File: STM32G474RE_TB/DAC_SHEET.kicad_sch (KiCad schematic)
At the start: 16 parts, among them U2 MCP4921-ESN, U3 MCP4921-ESN, U4 MCP4921-ESN, U5 OPA1678, U6 MCP4921-ESN, U7 REF3125, U9 OPA1678

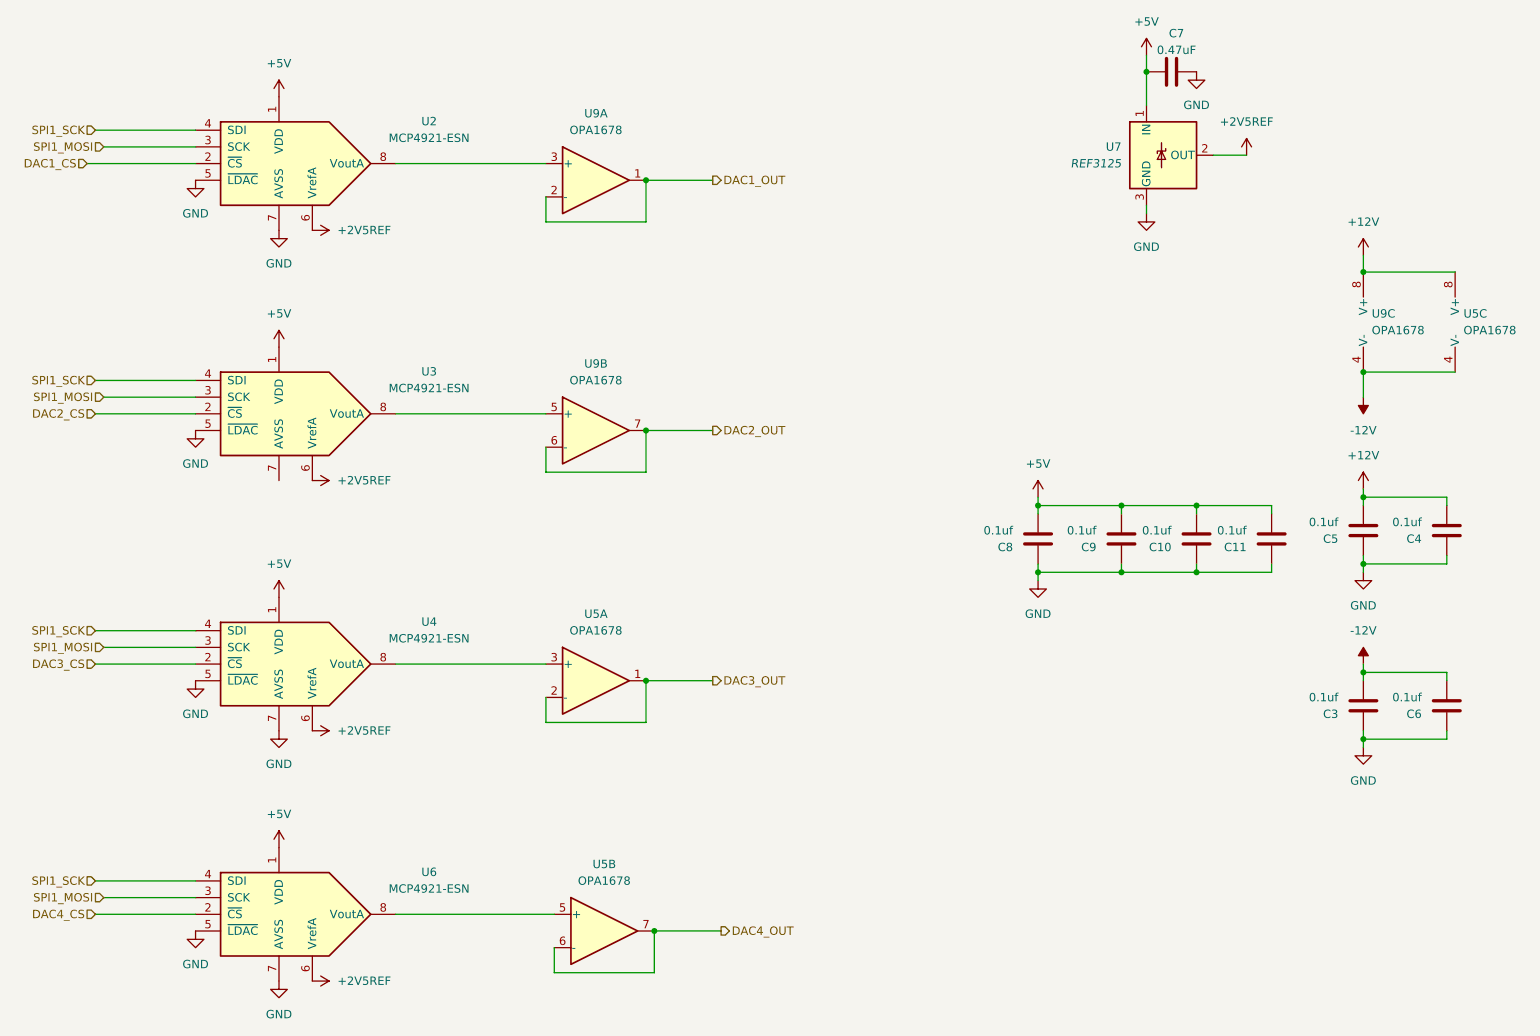
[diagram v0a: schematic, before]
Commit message: Added power LDO and built DAC buffer circuits Added pin descriptions
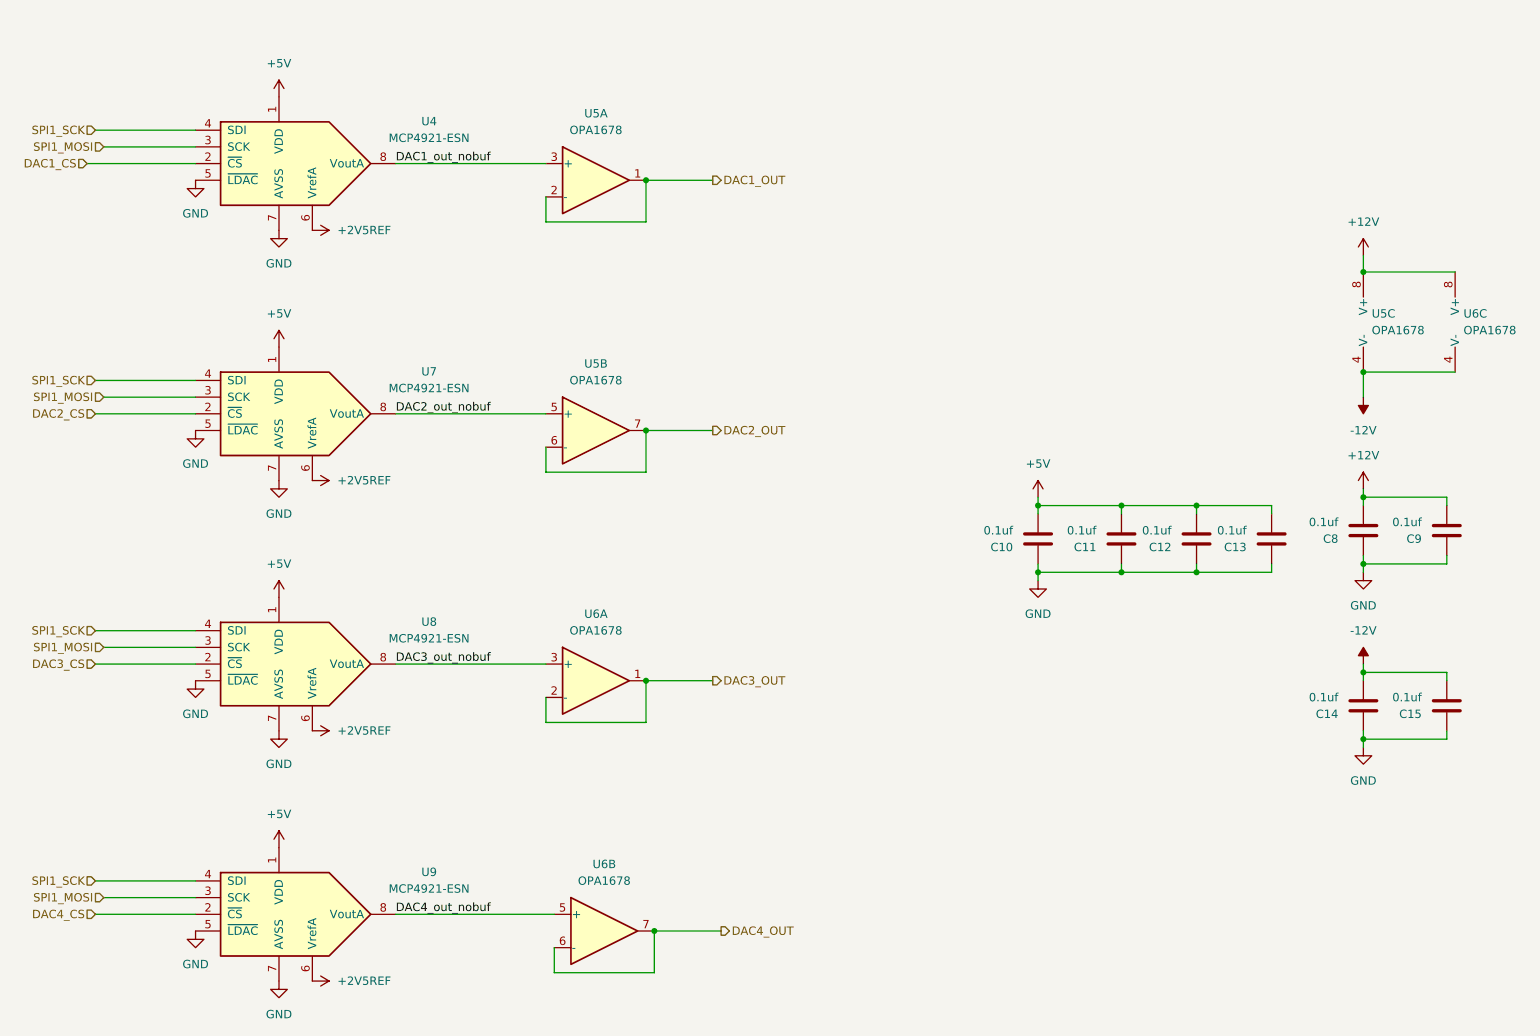
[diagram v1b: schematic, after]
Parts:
- removed C7: 0.47uF, Capacitor_SMD:C_0603_1608Metric, symbol Device:C
- removed U7: REF3125, Package_TO_SOT_SMD:SOT-23, symbol Reference_Voltage:REF3025
- renumbered C8 to C10, C9 to C11, C10 to C12, C11 to C13, C3 to C14, C6 to C15, C5 to C8, C4 to C9, U2 to U4, U9 to U5, U5 to U6, U3 to U7, U4 to U8, U6 to U9
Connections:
- net GND: now also U7.7 (AVSS)
- net DAC2_out_nobuf: now reaches U5.5 (+), U7.8 (VoutA)
- net DAC1_out_nobuf: now reaches U4.8 (VoutA), U5.3 (+)
- net DAC4_out_nobuf: now reaches U6.5 (+), U9.8 (VoutA)
- net DAC3_out_nobuf: now reaches U6.3 (+), U8.8 (VoutA)

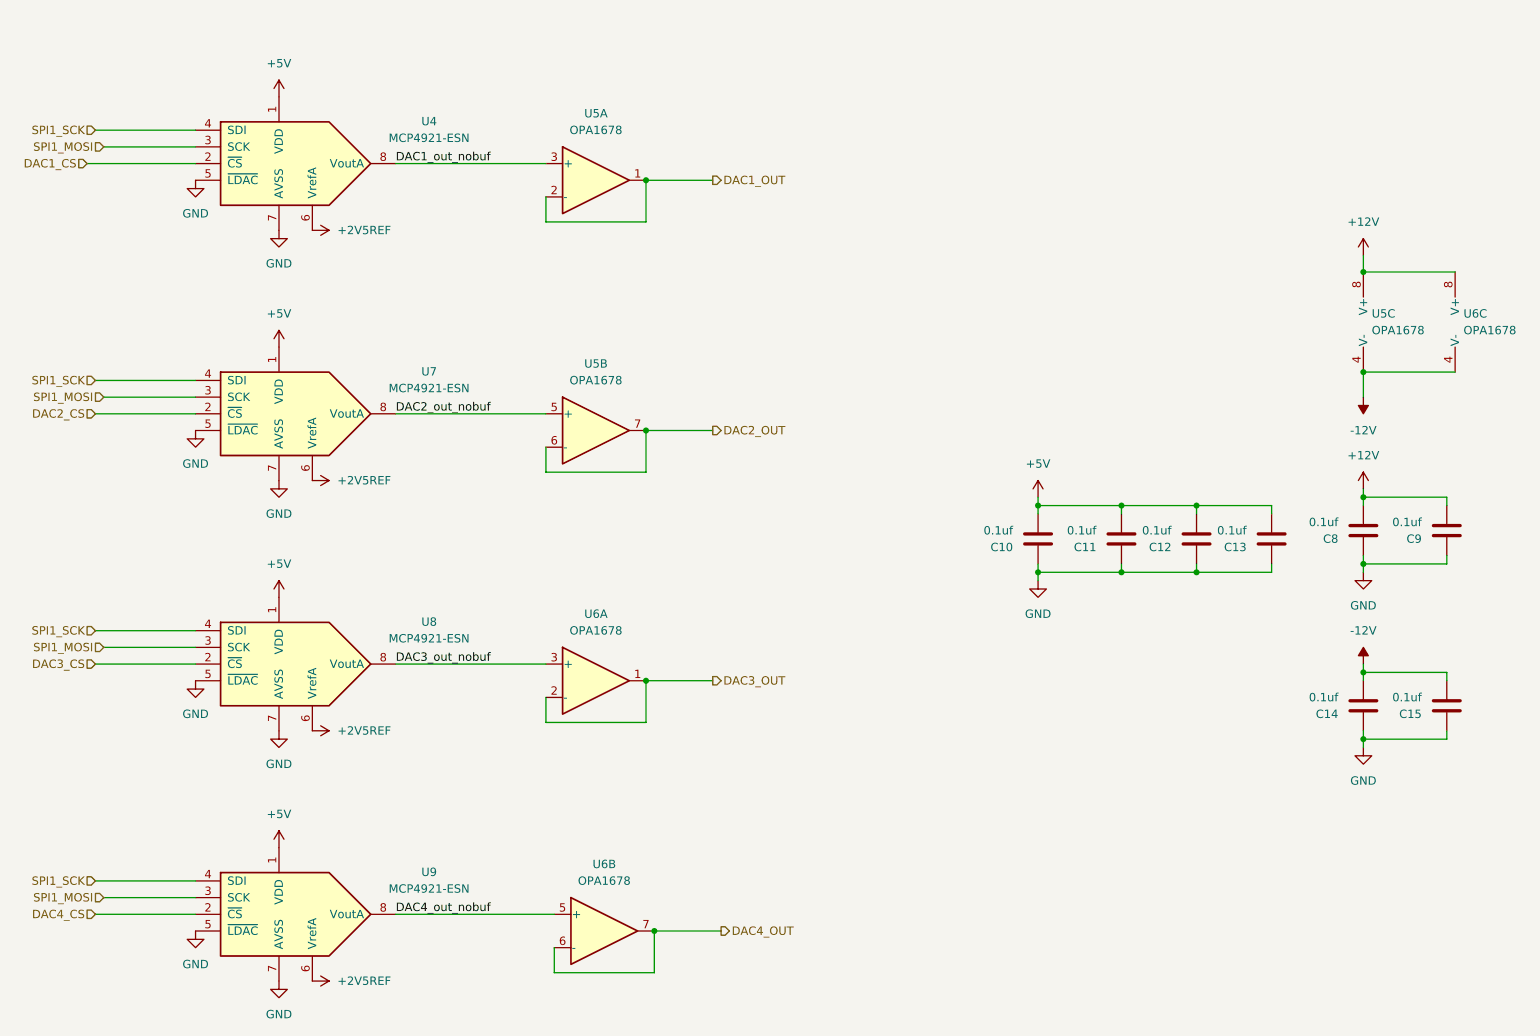
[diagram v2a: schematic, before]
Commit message: Added MOSFET template with led for debug or other functions
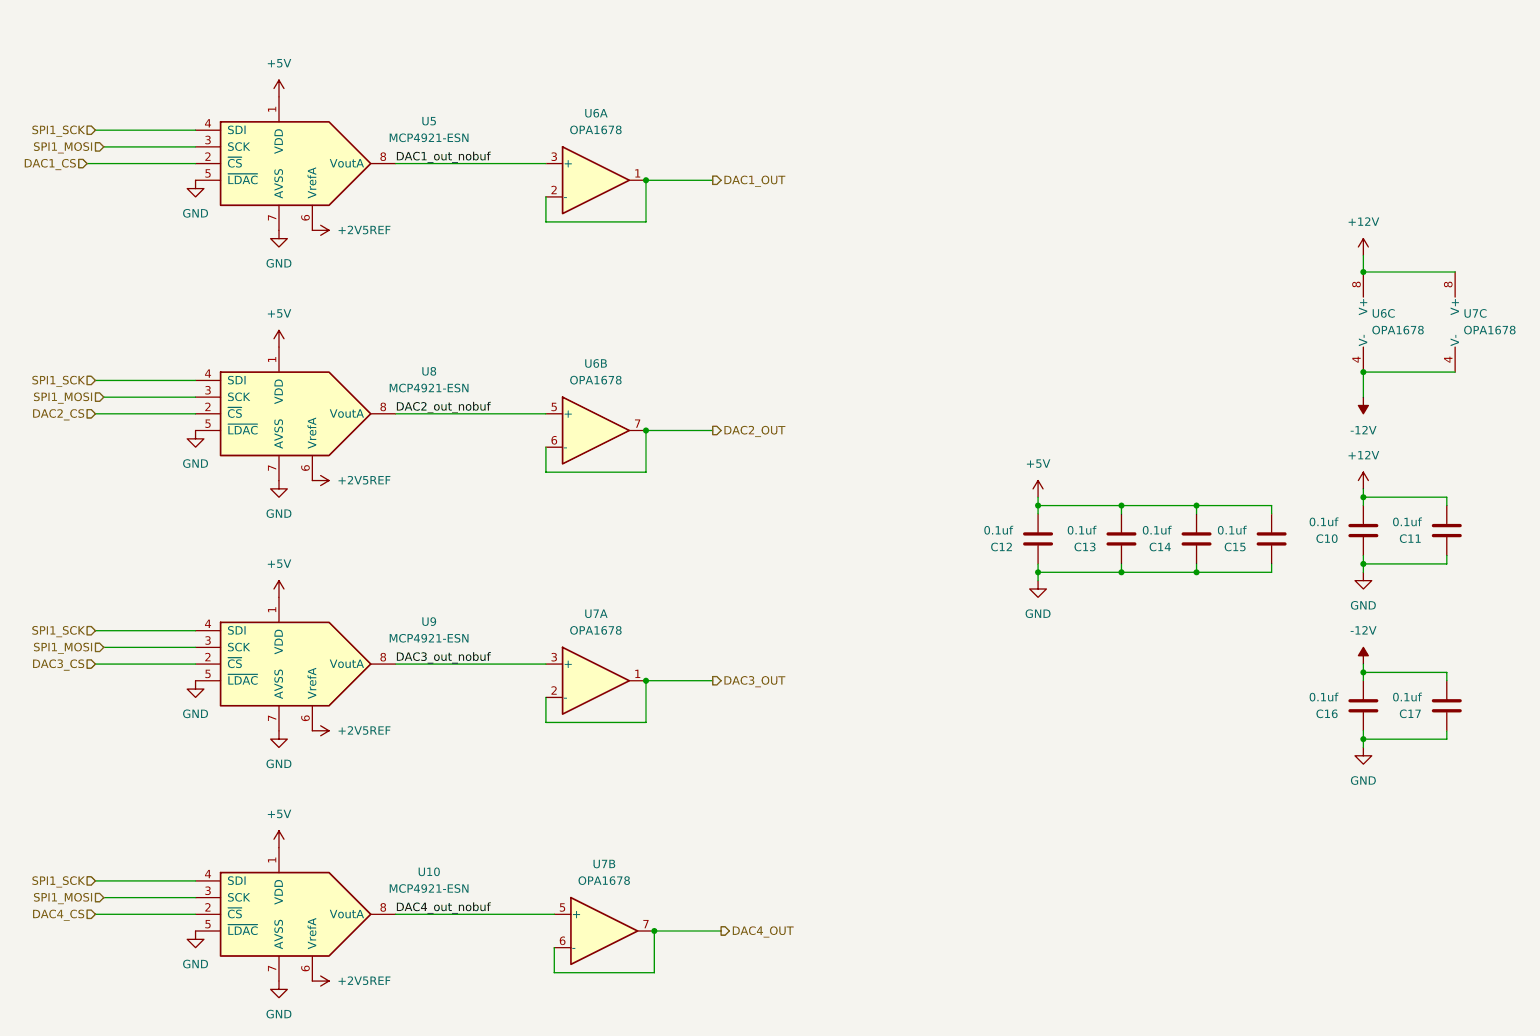
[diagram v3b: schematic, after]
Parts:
- renumbered C8 to C10, C9 to C11, C10 to C12, C11 to C13, C12 to C14, C13 to C15, C14 to C16, C15 to C17, U9 to U10, U4 to U5, U5 to U6, U6 to U7, U7 to U8, U8 to U9
